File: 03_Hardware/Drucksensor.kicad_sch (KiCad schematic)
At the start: 58 parts, among them J101 Conn_01x02, J102 Start, J103 RJ45, J104 RJ45, J105 DB15_Female_MountingHoles, J106 Serial, J107 Conn_01x03_Male, Q101 Q_NMOS_GSD, Q102 Q_NMOS_GSD, Q103 Q_NMOS_GSD, SW101 SW_DPST, SW102 SW_SPDT, U101 REF3040, U102 MAX232

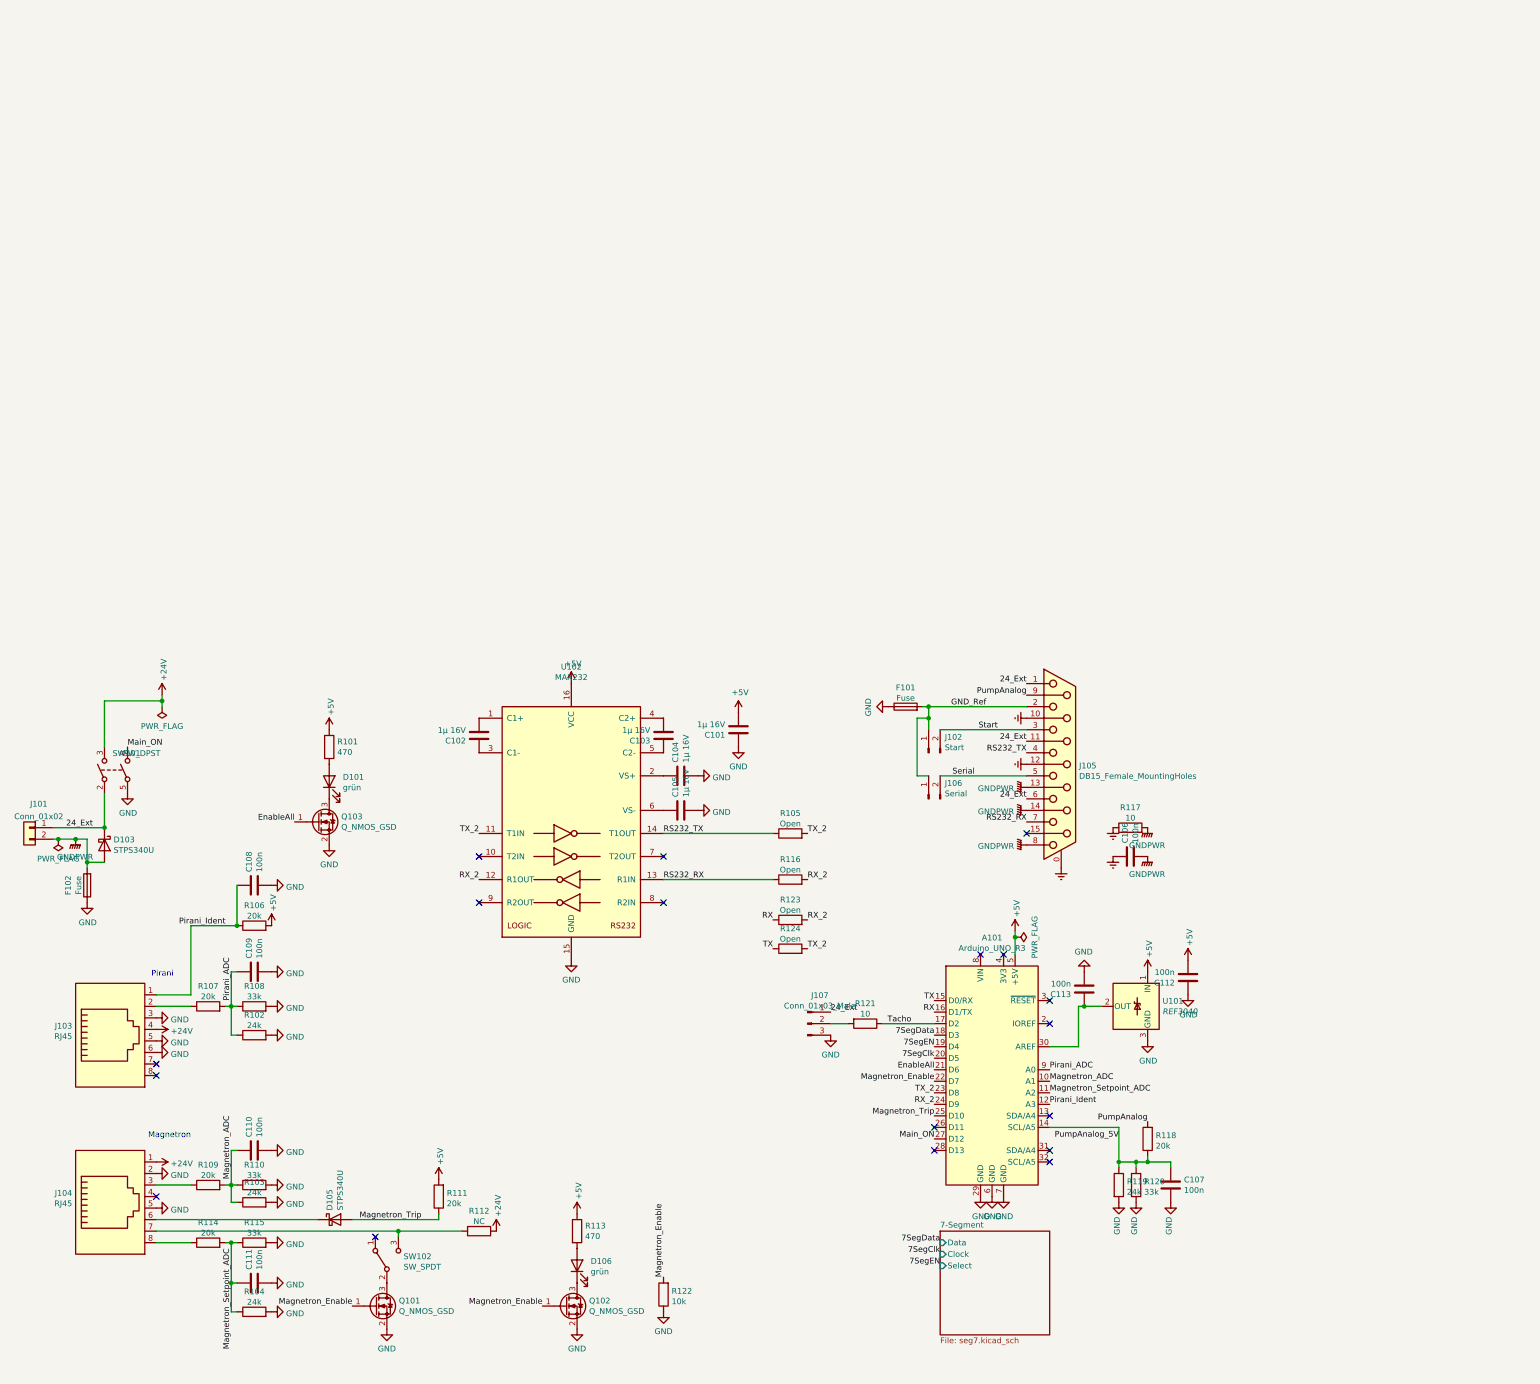
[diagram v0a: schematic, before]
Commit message: Anzeigeplan weiter, Datenblatt der 0,56" Anzeige dazugefügt
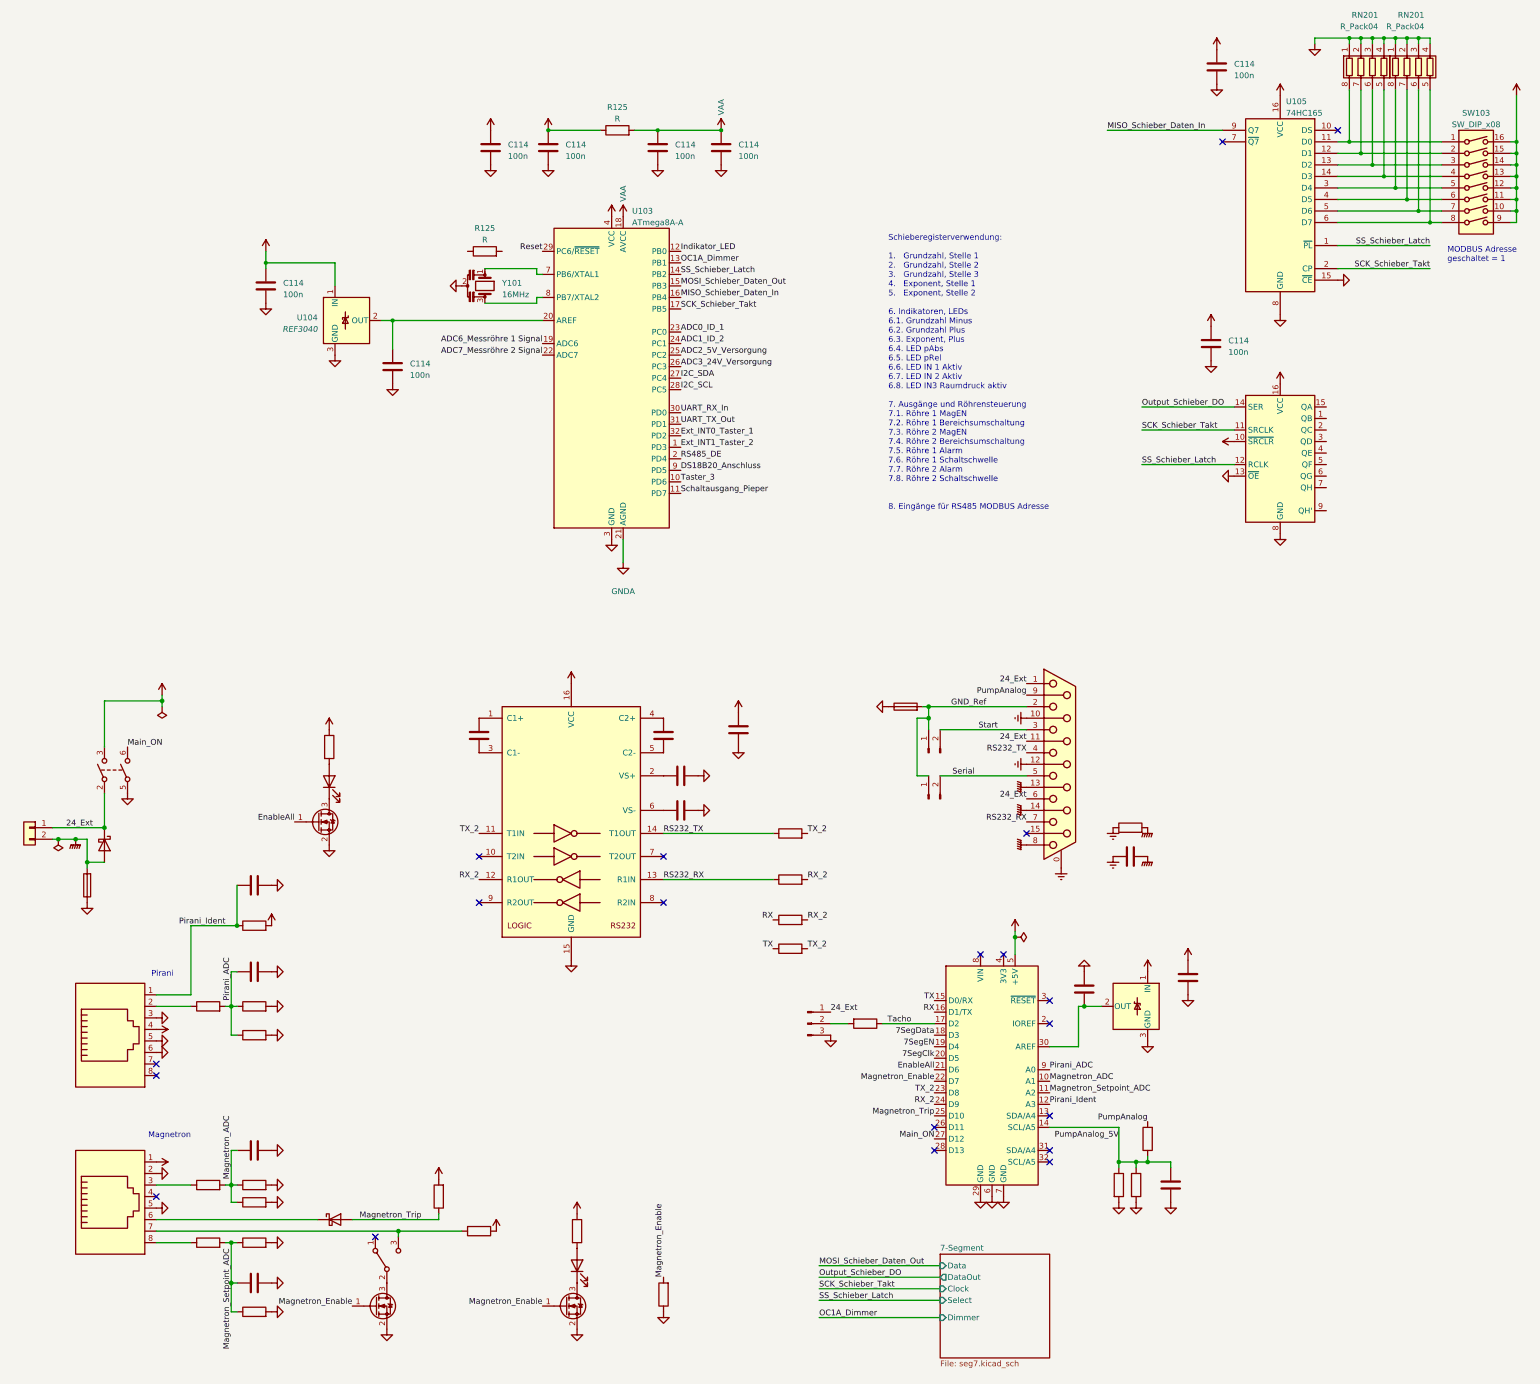
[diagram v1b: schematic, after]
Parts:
- added ?: (no value), symbol 74xx:74HC595
- added C114 (x8): 100n, symbol Device:C
- added R125 (x2): R, symbol Device:R
- added RN201 (x2): R_Pack04, symbol Device:R_Pack04
- added SW103: SW_DIP_x08, symbol Switch:SW_DIP_x08
- added U103: ATmega8A-A, Package_QFP:TQFP-32_7x7mm_P0.8mm, symbol MCU_Microchip_ATmega:ATmega8A-A
- added U104: REF3040, Package_TO_SOT_SMD:SOT-23, symbol Reference_Voltage:REF3040
- added U105: 74HC165, symbol 74xx:74HC165
- added Y101: 16MHz, symbol Device:Resonator
- ?: renamed from R104; value 24k -> (none); footprint Resistor_SMD:R_0603_1608Metric -> (none)
- ?: renamed from C110; value 100n -> (none); footprint Capacitor_SMD:C_0603_1608Metric -> (none)
- ?: renamed from R103; value 24k -> (none); footprint Resistor_SMD:R_0603_1608Metric -> (none)
- ?: renamed from R114; value 20k -> (none); footprint Resistor_SMD:R_0603_1608Metric -> (none)
- ?: renamed from Q101; value Q_NMOS_GSD -> (none); footprint Package_TO_SOT_SMD:SOT-23 -> (none)
- ?: renamed from J107; value Conn_01x03_Male -> (none); footprint Connector_PinSocket_2.54mm:PinSocket_1x03_P2.54mm_Vertical -> (none)
- ?: renamed from R115; value 33k -> (none); footprint Resistor_SMD:R_0603_1608Metric -> (none)
- ?: renamed from D101; value grün -> (none); footprint LED_SMD:LED_0603_1608Metric -> (none)
- ?: renamed from R116; value Open -> (none); footprint Resistor_SMD:R_0805_2012Metric -> (none)
- ?: renamed from R121; value 10 -> (none); footprint Resistor_SMD:R_0603_1608Metric -> (none)
- ?: renamed from D103; value STPS340U -> (none); footprint Diode_SMD:D_SMB -> (none)
- ?: renamed from F102; value Fuse -> (none); footprint Resistor_SMD:R_1210_3225Metric -> (none)
- ?: renamed from R108; value 33k -> (none); footprint Resistor_SMD:R_0603_1608Metric -> (none)
- ?: renamed from F101; value Fuse -> (none); footprint Resistor_SMD:R_1210_3225Metric -> (none)
- ?: renamed from R118; value 20k -> (none); footprint Resistor_SMD:R_0603_1608Metric -> (none)
- ?: renamed from C108; value 100n -> (none); footprint Capacitor_SMD:C_0603_1608Metric -> (none)
- ?: renamed from R102; value 24k -> (none); footprint Resistor_SMD:R_0603_1608Metric -> (none)
- ?: renamed from C112; value 100n -> (none); footprint Capacitor_SMD:C_0603_1608Metric -> (none)
- ?: renamed from D106; value grün -> (none); footprint LED_SMD:LED_0603_1608Metric -> (none)
- ?: renamed from D105; value STPS340U -> (none); footprint Diode_SMD:D_SMB -> (none)
- ?: renamed from R123; value Open -> (none); footprint Resistor_SMD:R_0805_2012Metric -> (none)
- ?: renamed from R106; value 20k -> (none); footprint Resistor_SMD:R_0603_1608Metric -> (none)
- ?: renamed from R120; value 33k -> (none); footprint Resistor_SMD:R_0603_1608Metric -> (none)
- ?: renamed from J102; value Start -> (none); footprint Connector_PinSocket_2.54mm:PinSocket_1x02_P2.54mm_Vertical -> (none)
- ?: renamed from C101; value 1µ 16V -> (none); footprint Capacitor_SMD:C_0805_2012Metric -> (none)
- ?: renamed from J106; value Serial -> (none); footprint Connector_PinSocket_2.54mm:PinSocket_1x02_P2.54mm_Vertical -> (none)
- ?: renamed from U102; value MAX232 -> (none); footprint Package_SO:SOIC-16W_7.5x10.3mm_P1.27mm -> (none)
- ?: renamed from U101; value REF3040 -> (none); footprint Package_TO_SOT_SMD:SOT-23 -> (none)
- ?: renamed from Q102; value Q_NMOS_GSD -> (none); footprint Package_TO_SOT_SMD:SOT-23 -> (none)
- ?: renamed from C106; value 100n -> (none); footprint Capacitor_SMD:C_0603_1608Metric -> (none)
- ?: renamed from C105; value 1µ 16V -> (none); footprint Capacitor_SMD:C_0805_2012Metric -> (none)
- ?: renamed from C104; value 1µ 16V -> (none); footprint Capacitor_SMD:C_0805_2012Metric -> (none)
- ?: renamed from A101; value Arduino_UNO_R3 -> (none); footprint Module:Arduino_UNO_R3 -> (none)
- ?: renamed from R107; value 20k -> (none); footprint Resistor_SMD:R_0603_1608Metric -> (none)
- ?: renamed from R105; value Open -> (none); footprint Resistor_SMD:R_0805_2012Metric -> (none)
- ?: renamed from R122; value 10k -> (none); footprint Resistor_SMD:R_0603_1608Metric -> (none)
- ?: renamed from R110; value 33k -> (none); footprint Resistor_SMD:R_0603_1608Metric -> (none)
- ?: renamed from J101; value Conn_01x02 -> (none); footprint TerminalBlock:TerminalBlock_bornier-4_P5.08mm -> (none)
- ?: renamed from R109; value 20k -> (none); footprint Resistor_SMD:R_0603_1608Metric -> (none)
- ?: renamed from R112; value NC -> (none); footprint Resistor_SMD:R_0603_1608Metric -> (none)
- ?: renamed from Q103; value Q_NMOS_GSD -> (none); footprint Package_TO_SOT_SMD:SOT-23 -> (none)
- ?: renamed from R117; value 10 -> (none); footprint Resistor_SMD:R_0603_1608Metric -> (none)
- ?: renamed from C111; value 100n -> (none); footprint Capacitor_SMD:C_0603_1608Metric -> (none)
- ?: renamed from R124; value Open -> (none); footprint Resistor_SMD:R_0805_2012Metric -> (none)
- ?: renamed from C102; value 1µ 16V -> (none); footprint Capacitor_SMD:C_0805_2012Metric -> (none)
- ?: renamed from R111; value 20k -> (none); footprint Resistor_SMD:R_0603_1608Metric -> (none)
- ?: renamed from R101; value 470 -> (none); footprint Resistor_SMD:R_0603_1608Metric -> (none)
- ?: renamed from J104; value RJ45 -> (none); footprint Sven:RJ45_Amphenol_54602_mod -> (none)
- ?: renamed from C107; value 100n -> (none); footprint Capacitor_SMD:C_0603_1608Metric -> (none)
- ?: renamed from C103; value 1µ 16V -> (none); footprint Capacitor_SMD:C_0805_2012Metric -> (none)
- ?: renamed from C109; value 100n -> (none); footprint Capacitor_SMD:C_0603_1608Metric -> (none)
- ?: renamed from SW102; value SW_SPDT -> (none); footprint Sven:Switch_DPDT -> (none)
- ?: renamed from J103; value RJ45 -> (none); footprint Sven:RJ45_Amphenol_54602_mod -> (none)
- ?: renamed from C113; value 100n -> (none); footprint Capacitor_SMD:C_0603_1608Metric -> (none)
- ?: renamed from J105; value DB15_Female_MountingHoles -> (none); footprint Connector_Dsub:DSUB-15_Female_Vertical_P2.77x2.84mm_MountingHoles -> (none)
- ?: renamed from R119; value 24k -> (none); footprint Resistor_SMD:R_0603_1608Metric -> (none)
- ?: renamed from R113; value 470 -> (none); footprint Resistor_SMD:R_0603_1608Metric -> (none)
- ?: renamed from SW101; value SW_DPST -> (none); footprint Sven:Switch_DPDT -> (none)
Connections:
- net +5V: now also ?.10 (~{SRCLR}), ?.16 (VCC), C114.1, C114.1, C114.1, C114.1, C114.1, R125.1, SW103.10, SW103.11, SW103.12, SW103.13, SW103.14, SW103.15, SW103.16, SW103.9, U103.4 (VCC), U103.6 (VCC), U104.1 (IN), U105.16 (VCC)
- net GND: now also ?.13 (~{OE}), ?.8 (GND), C114.2, C114.2, C114.2, C114.2, C114.2, C114.2, C114.2, C114.2, RN201.1 (R1.1), RN201.1 (R1.1), RN201.2 (R2.1), RN201.2 (R2.1), RN201.3 (R3.1), RN201.3 (R3.1), RN201.4 (R4.1), RN201.4 (R4.1), U103.3 (GND), U103.5 (GND), U104.3 (GND), U105.15 (~{CE}), U105.8 (GND), Y101.2
- new net: C114.1, U103.20 (AREF), U104.2 (OUT)
- new net: U103.7 (PB6/XTAL1), Y101.1
- new net: U103.8 (PB7/XTAL2), Y101.3
- new net: RN201.8 (R1.2), SW103.1, U105.11 (D0)
- new net: RN201.7 (R2.2), SW103.2, U105.12 (D1)
- new net: RN201.6 (R3.2), SW103.3, U105.13 (D2)
- new net: RN201.5 (R4.2), SW103.4, U105.14 (D3)
- new net: RN201.8 (R1.2), SW103.5, U105.3 (D4)
- new net: RN201.7 (R2.2), SW103.6, U105.4 (D5)
- new net: RN201.6 (R3.2), SW103.7, U105.5 (D6)
- new net: RN201.5 (R4.2), SW103.8, U105.6 (D7)
- new net ADC0_ID_1: U103.23 (PC0)
- new net ADC1_ID_2: U103.24 (PC1)
- new net ADC2_5V_Versorgung: U103.25 (PC2)
- new net ADC3_24V_Versorgung: U103.26 (PC3)
- new net ADC6_Messröhre 1 Signal: U103.19 (ADC6)
- new net ADC7_Messröhre 2 Signal: U103.22 (ADC7)
- new net DS18B20_Anschluss: U103.9 (PD5)
- new net Ext_INT0_Taster_1: U103.32 (PD2)
- new net Ext_INT1_Taster_2: U103.1 (PD3)
- new net GNDA: U103.21 (AGND)
- new net I2C_SCL: U103.28 (PC5)
- new net I2C_SDA: U103.27 (PC4)
- new net Indikator_LED: U103.12 (PB0)
- new net MISO_Schieber_Daten_In: U103.16 (PB4), U105.9 (Q7)
- new net MOSI_Schieber_Daten_Out: U103.15 (PB3)
- new net OC1A_Dimmer: U103.13 (PB1)
- new net Output_Schieber_DO: ?.14 (SER)
- new net RS485_DE: U103.2 (PD4)
- new net Reset: U103.29 (PC6/~{RESET})
- new net SCK_Schieber_Takt: ?.11 (SRCLK), U103.17 (PB5), U105.2 (CP)
- new net SS_Schieber_Latch: ?.12 (RCLK), U103.14 (PB2), U105.1 (~{PL})
- new net Schaltausgang_Pieper: U103.11 (PD7)
- new net Taster_3: U103.10 (PD6)
- new net UART_RX_In: U103.30 (PD0)
- new net UART_TX_Out: U103.31 (PD1)
- new net VAA: C114.1, C114.1, R125.2, U103.18 (AVCC)
- no-connect marks 18 -> 20
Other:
- sheet 7-Segment ports: added DataOut, Dimmer; removed none
- note added: "MODBUS Adresse geschaltet = 1"
- note added: "Schieberegisterverwendung: 1. Grundzahl, Stelle 1 2. Grundzahl, Stelle 2 3. Grundzahl, Stelle 3 4. Exponent, Stelle 1 5. Exponent, Stelle 2 6. Indikatoren, LEDs 6.1. Grundzahl Minus 6.2. Grundzahl Plus 6.3. Exponent, Plus 6.4. LED pAbs 6.5. LED pRel 6.6. LED IN 1 Aktiv 6.7. LED IN 2 Aktiv 6.8. LED IN3 Raumdruck aktiv 7. Ausgänge und Röhrensteuerung 7.1. Röhre 1 MagEN 7.2. Röhre 1 Bereichsumschalt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"

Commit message: Schaltplan Main erweitert und PSU/Ausgänge hinzugefügt
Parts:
- removed ?: (no value), symbol Device:LED
- removed ?: (no value), symbol Device:Q_NMOS_GSD
- removed ?: (no value), symbol Device:R
- removed ?: (no value), symbol Switch:SW_DPST
- added ? (x2): (no value), symbol Connector:RJ45
- added C114 (x3): 100n, symbol Device:C
- added NT101: Massesternpunkt, symbol Device:NetTie_2
- added R125: R, symbol Device:R
- added U107: SN75176AD, Package_SO:SOIC-8_3.9x4.9mm_P1.27mm, symbol Interface_UART:SN75176AD
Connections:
- net +24V: now also ?.1, ?.1 (K), ?.1, ?.1
- net +5V: now also R125.1, ?.6, ?.6, C114.1, R125.2, U107.8 (VCC); no longer C114.1, U104.1 (IN)
- net 24_Ext: no longer ?.1 (K), ?.1 (Pin_1)
- net GND: now also ?.2 (A), ?.2 (Pin_2), ?.2, ?.2, C114.1, C114.2, NT101.2, U107.5 (GND); no longer ?.1, C114.2, C114.2, U104.3 (GND)
- net GNDA: now also C114.2, C114.2, U104.3 (GND), C114.2, NT101.1
- net GNDPWR: no longer ?.2, ?.2 (A), ?.2 (Pin_2)
- net RS485_DE: now also U107.2 (~{RE}), U107.3 (DE)
- net Reset: now also R125.2, C114.2
- net UART_RX_In: now also U107.1 (R)
- net UART_TX_Out: now also U107.4 (D)
- net R1_Bereich: now reaches ?.1 (QB)
- net R1_MagEn: now reaches ?.15 (QA)
- net R2_MagEn: now reaches ?.2 (QC)
- net R2_Bereich: now reaches ?.3 (QD)
- net Schaltausgänge/R1_Alarm: now reaches ?.4 (QE)
- net Schaltausgänge/R1_Schwelle: now reaches ?.5 (QF)
- net Schaltausgänge/R2_Alarm: now reaches ?.6 (QG)
- net Schaltausgänge/R2_Schwelle: now reaches ?.7 (QH)
- new net: C114.1, C114.1, R125.1, U104.1 (IN)
- new net: ?.7, ?.7
- new net: ?.8, ?.8
- new net: ?.1 (Pin_1), ?.2
- new net RS485_A: ?.5, ?.5, U107.6 (A)
- new net RS485_B: ?.4, ?.4, U107.7 (B)
- no-connect marks 20 -> 23
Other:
- added sheet 5V-Versorgung (PSU.kicad_sch)
- added sheet Schaltausgänge (digital_out.kicad_sch)
- note added: "Kommunikationsschnittstelle"
- company: (none) -> Institut für theoretischen Igorismus
- title: (none) -> Vakkumanzeige für zwei aktive Vakuumsensoren
- moved on the sheet: C114, R125, RN201, SW103, U103, U104, U105, Y101

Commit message: Schaltplan erweitert, I2C eingebaut
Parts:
- added C125 (x4): 100p, symbol Device:C
- added D101: SP0502BAHT, Package_TO_SOT_SMD:SOT-23, symbol Power_Protection:SP0502BAHT
- added J110: DS18B20, symbol Connector_Generic:Conn_01x03
- added J111: Conn_01x06_Male, symbol Connector:Conn_01x06_Male
- added JP101 (x2): Jumper_2_Open, symbol Jumper:Jumper_2_Open
- added JP103: WP_OFF, symbol Jumper:Jumper_2_Open
- added R127 (x8): 100k, symbol Device:R
- added TP101 (x2): TestPoint, symbol Connector:TestPoint
- added U108: CAT24M01W, Package_SO:SOIC-8_3.9x4.9mm_P1.27mm, symbol Memory_EEPROM:CAT24M01W
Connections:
- net +24V: now also JP101.1 (A), R127.1; no longer ?.1, ?.1
- net +5V: now also J110.1 (Pin_1), JP101.1 (A), R127.1, R127.2, R127.2, U108.8 (VCC); no longer ?.6, ?.6
- net ADC2_5V_Versorgung: now also C125.1, R127.1, R127.2
- net ADC3_24V_Versorgung: now also C125.1, R127.1, R127.2
- net DS18B20_Anschluss: now also J110.2 (Pin_2), R127.1
- net GND: now also C125.2, C125.2, C125.2, C125.2, D101.3 (A), J110.3 (Pin_3), J111.2 (Pin_2), JP103.1 (A), R127.2, R127.2, R127.2, R127.2, U108.4 (GND)
- net I2C_SCL: now also J111.3 (Pin_3), U108.6 (SCL)
- net I2C_SDA: now also J111.4 (Pin_4), U108.5 (SDA)
- net RS485_A: now also C125.1, D101.1 (K), R127.1
- net RS485_B: now also C125.1, D101.2 (K), R127.1
- net at ?.7, ?.7: now also TP101.1
- net at ?.8, ?.8: now also TP101.1
- new net: ?.1, ?.1, JP101.2 (B)
- new net: ?.6, ?.6, JP101.2 (B)
- new net: JP103.2 (B), R127.1, U108.7 (WP)
- new net +3V3: J111.1 (Pin_1)
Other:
- sheet 5V-Versorgung renamed Kleinspannungsversorgung
- sheet Kleinspannungsversorgung ports: added 3,3V; removed none
- note added: "Kommunikationsschnittstelle: Achtung: RS485 ist nicht intern terminiert!"
- note added: "Vref = 4,096V"
- note removed: "Kommunikationsschnittstelle"
- moved on the sheet: C114, R125, U104, U107
